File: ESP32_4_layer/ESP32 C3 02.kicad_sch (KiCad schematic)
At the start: 5 parts, among them J3 GSD090012SEU_SDcard_Connector, U2 ESP32-C3-WROOM-02, U3 CP2102N-Axx-xQFN20, U4 USBLC6-2SC6, U5 W25Q32JVSS

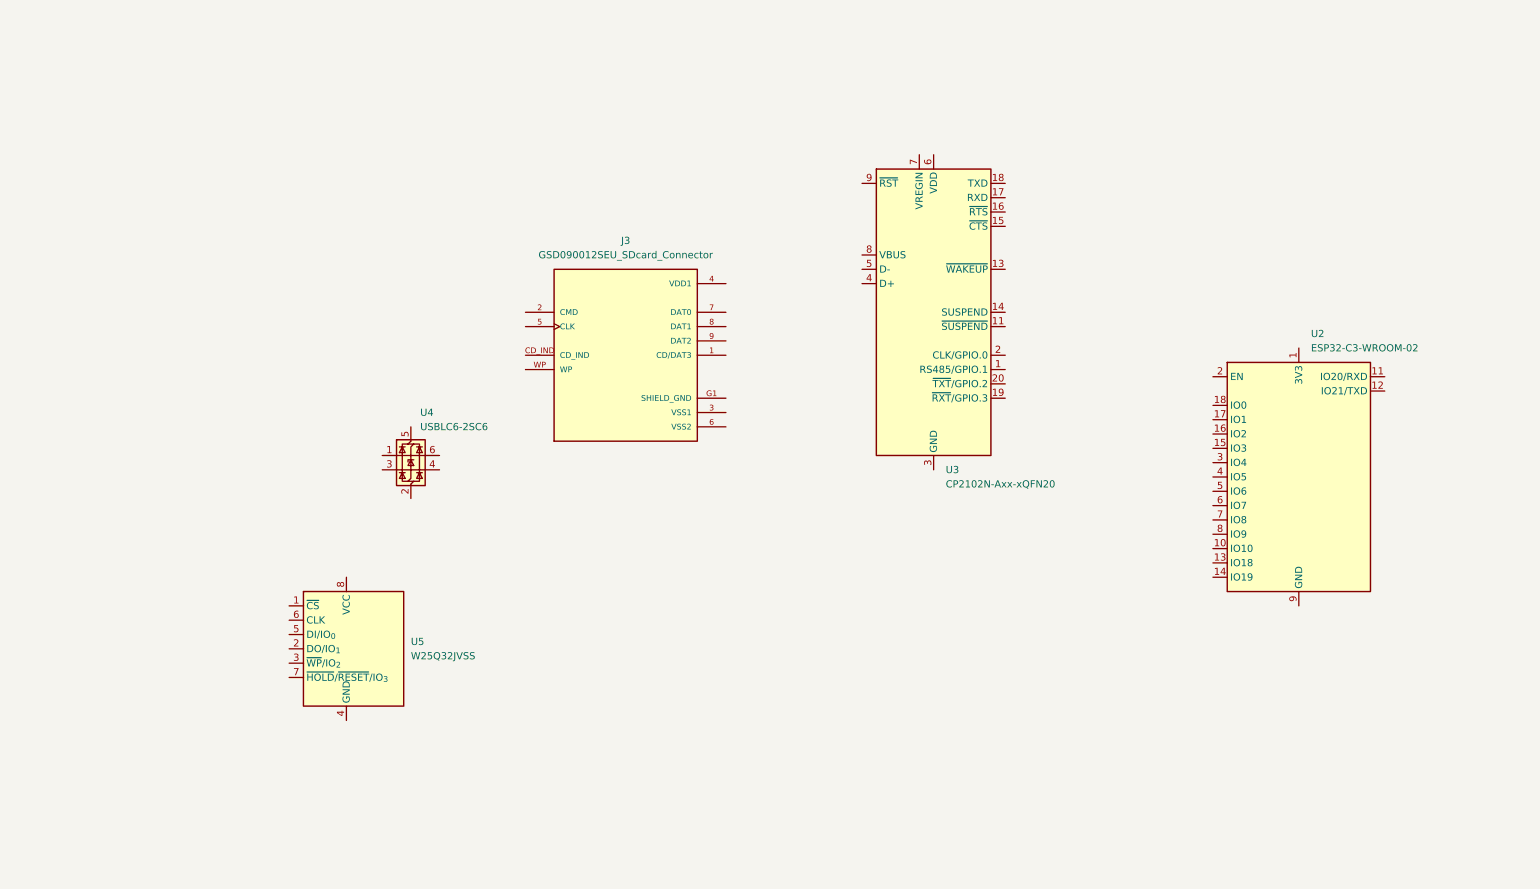
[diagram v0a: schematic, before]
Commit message: usb to uart converter schematic completed
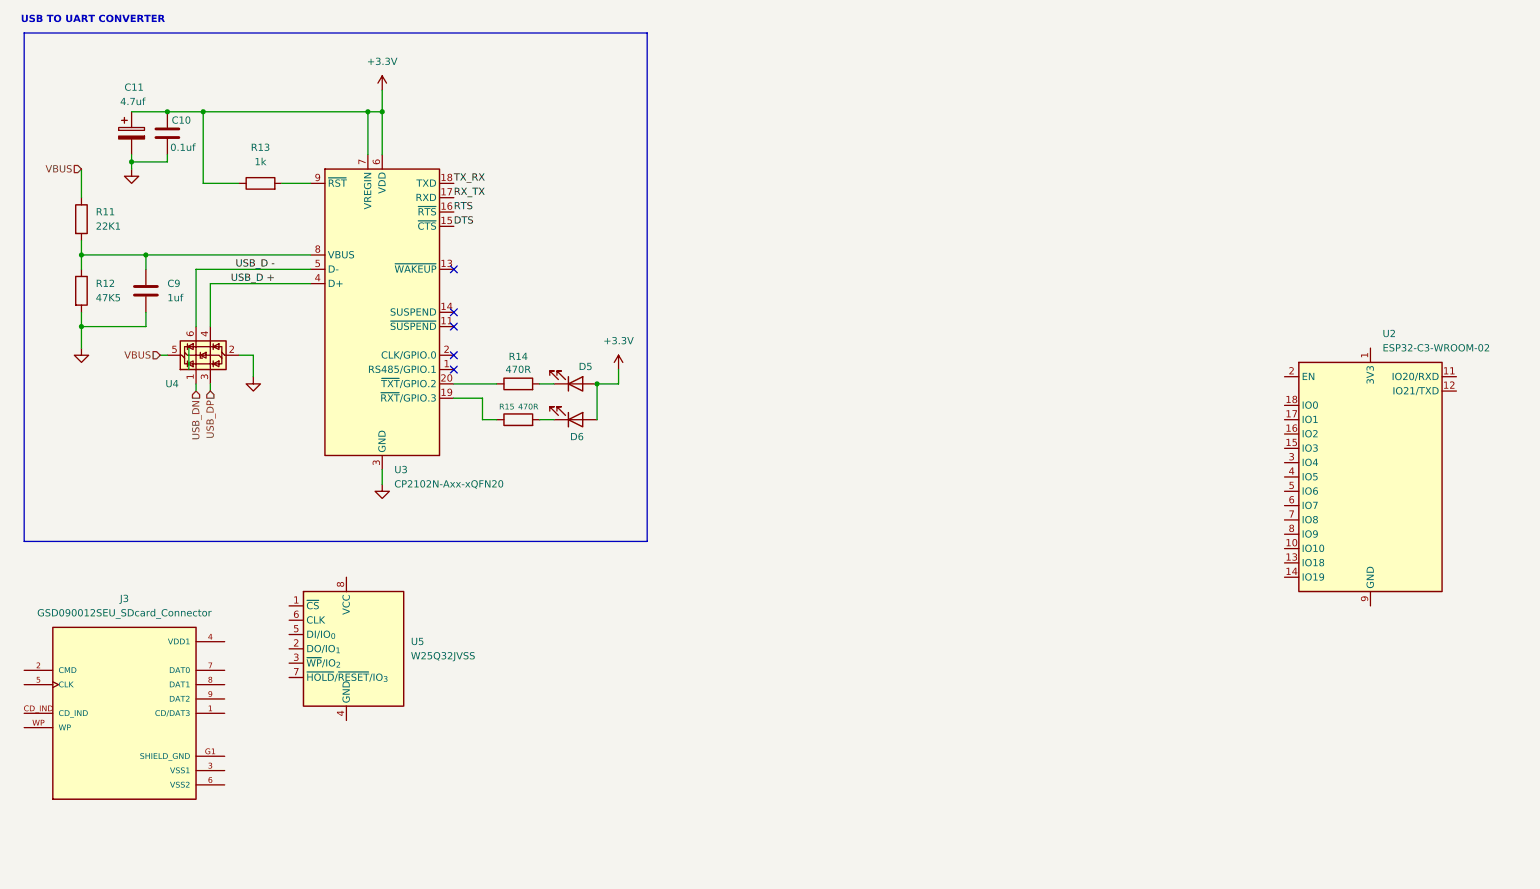
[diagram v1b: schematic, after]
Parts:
- added C10: 0.1uf, symbol Device:C
- added C11: 4.7uf, symbol Device:C_Polarized
- added C9: 1uf, symbol Device:C
- added D5, D6: LED, symbol Device:LED
- added R11: 22K1, symbol Device:R
- added R12: 47K5, symbol Device:R
- added R13: 1k, symbol Device:R
- added R14, R15: 470R, symbol Device:R
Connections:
- net GND: now reaches U3.12 (GND), U3.21 (GND), U3.3 (GND)
- net GND: now also U4.2 (GND), C10.2, C11.2, C9.2, R12.2
- net DTS: now reaches U3.15 (~{CTS})
- net RTS: now reaches U3.16 (~{RTS})
- net RX_TX: now reaches U3.17 (RXD)
- net TX_RX: now reaches U3.18 (TXD)
- net at U3.19 (~{RXT}/GPIO.3): now also R15.1
- net at U3.20 (~{TXT}/GPIO.2): now also R14.1
- net USB_D +: now reaches U3.4 (D+)
- net USB_D +: now also U4.4 (I/O2)
- net USB_D -: now reaches U3.5 (D-)
- net USB_D -: now also U4.6 (I/O1)
- net +3.3V: now reaches U3.6 (VDD)
- net +3.3V: now also U3.7 (VREGIN), C10.1, C11.1, D5.2 (A), D6.2 (A), R13.1
- net at U3.8 (VBUS): now also C9.1, R11.2, R12.1
- net at U3.9 (~{RST}): now also R13.2
- net USB_DN: now reaches U4.1 (I/O1)
- net USB_DP: now reaches U4.3 (I/O2)
- net VBUS: now reaches U4.5 (VBUS)
- net VBUS: now also R11.1
- new net: D5.1 (K), R14.2
- new net: D6.1 (K), R15.2
- no-connect marks 0 -> 5
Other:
- note added: "USB TO UART CONVERTER"
- moved on the sheet: J3, U2, U3, U4

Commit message: MCU and SD CARD schematic completed
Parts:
- removed U2: ESP32-C3-WROOM-02, RF_Module:ESP32-C3-WROOM-02, symbol RF_Module:ESP32-C3-WROOM-02
- added C12, C14: 10uf, symbol Device:C_Polarized
- added C13, C15: 0.1uf, symbol Device:C
- added R16: R15, symbol Device:R
- added R17, R19: 50R, symbol Device:R
- added R18: 10K, symbol Device:R
- added U2: ESP32-C3-WROOM-02-H4, ESP32-C3-WROOM-02-H4:MODULE_ESP32-C3-WROOM-02-H4, symbol Own_Library:ESP32-C3-WROOM-02-H4
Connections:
- net SHIELD_GND is gone; now on net GND: J3.G1 (SHIELD_GND), J3.G2 (SHIELD_GND), J3.G3 (SHIELD_GND), J3.G4 (SHIELD_GND)
- net +3.3V: now also J3.4 (VDD1), C12.1, C13.1, C14.1, C15.1, R18.2, U2.1 (3V3)
- net GND: now also J3.3 (VSS1), J3.6 (VSS2), J3.8 (DAT1), J3.9 (DAT2), C12.2, C13.2, C14.2, C15.2, U2.19 (GND), U2.20 (GND), U2.21 (GND), U2.22 (GND), U2.23 (GND), U2.24 (GND), U2.25 (GND), U2.26 (GND), U2.27 (GND), U2.28 (GND), U2.29 (GND), U2.30 (GND), U2.31 (GND), U2.32 (GND), U2.33 (GND), U2.34 (GND), U2.35 (GND), U2.36 (GND), U2.37 (GND), U2.38 (GND), U2.39 (GND), U2.9 (GND)
- net RX_TX: now also U2.12 (TXD)
- net TX_RX: now also U2.11 (RXD)
- net CS_SD: now reaches J3.1 (CD/DAT3)
- net CS_SD: now also U2.18 (IO0)
- net MOSI_DI: now reaches J3.2 (CMD)
- net MOSI_DI: now also R17.2
- net SCLK: now reaches J3.5 (CLK)
- net SCLK: now also R16.1
- net at J3.7 (DAT0): now also R19.1
- new net: R17.1, U2.6 (IO7)
- new net: R16.2, U2.5 (IO6)
- new net BOOT: U2.8 (IO9)
- new net CS: U2.10 (IO10)
- new net EN: U2.2 (EN)
- new net GPIO18: U2.13 (IO18)
- new net GPIO19: U2.14 (IO19)
- new net GPIO8: U2.7 (IO8)
- new net MIC_OUT: U2.4 (IO5)
- new net MISO_DO: R19.2, U2.16 (IO2)
- new net PHOTO_C: U2.17 (IO1)
- new net SCL: U2.15 (IO3)
- new net SDA: U2.3 (IO4)
- no-connect marks 5 -> 7
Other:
- note added: "MCU"
- note added: "SD CARD"
- moved on the sheet: J3, U5

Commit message: FLASH AND TEST POINTS
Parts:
- added C16: 0.1uf, symbol Device:C
- added R20: 50R, symbol Device:R
- added TP1, TP2, TP3, TP4, TP5: TestPoint, symbol Connector:TestPoint
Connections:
- net +3.3V: now also U5.3 (~{WP}/IO_{2}), U5.7 (~{HOLD}/~{RESET}/IO_{3}), U5.8 (VCC), C16.1
- net CS: now also U5.1 (~{CS}), TP4.1
- net CS_SD: now also TP5.1
- net GND: now also U5.4 (GND), C16.2
- net MISO_DO: now also R20.1, TP1.1
- net MOSI_DI: now also U5.5 (DI/IO_{0}), TP2.1
- net SCLK: now also U5.6 (CLK), TP3.1
- net at U5.2 (DO/IO_{1}): now also R20.2
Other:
- added sheet Sensors (Sensors.kicad_sch)
- added sheet User Interface (User_Interface.kicad_sch)
- note added: "FLASH MEMORY"
- note added: "TEST POINTS"
- title: (none) -> ESP32 C3, USB to UART, SD CARD and FLASH
- moved on the sheet: C15, U5

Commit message: SENSORS COMPLETED
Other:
- sheet Sensors ports: added MIC_OUT, PHOTO_C, SCL, SDA; removed none
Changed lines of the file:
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@@
 	(wire
 		(pts
+			(xy 262.89 125.73) (xy 260.35 125.73)
+		)
+		(stroke
+			(width 0)
+			(type default)
+		)
+	)
+	(wire
+		(pts
 			(xy 205.74 156.21) (xy 205.74 152.4)
 		)
@@
 	(wire
 		(pts
+			(xy 262.89 133.35) (xy 260.35 133.35)
+		)
+		(stroke
+			(width 0)
+			(type default)
+		)
+	)
+	(wire
+		(pts
 			(xy 203.2 48.26) (xy 210.82 48.26)
 		)
@@
 	(wire
 		(pts
+			(xy 262.89 128.27) (xy 260.35 128.27)
+		)
+		(stroke
+			(width 0)
+			(type default)
+		)
+	)
+	(wire
+		(pts
 			(xy 48.26 41.91) (xy 48.26 43.18)
 		)
@@
 	(wire
 		(pts
+			(xy 262.89 130.81) (xy 260.35 130.81)
+		)
+		(stroke
+			(width 0)
+			(type default)
+		)
+	)
+	(wire
+		(pts
 			(xy 48.26 34.29) (xy 54.61 34.29)
 		)
@@
 		)
 	)
+	(label "SDA"
+		(at 262.89 133.35 0)
+		(effects
+			(font
+				(size 1.27 1.27)
+				(thickness 0.254)
+				(bold yes)
+			)
+			(justify left bottom)
+		)
+	)
+	(label "MIC_OUT"
+		(at 262.89 125.73 0)
+		(effects
+			(font
+				(size 1.27 1.27)
+				(thickness 0.254)
+				(bold yes)
+			)
+			(justify left bottom)
+		)
+	)
 	(label "GPIO18"
 		(at 203.2 58.42 0)
@@
 		)
 	)
+	(label "SCL"
+		(at 262.89 130.81 0)
+		(effects
+			(font
+				(size 1.27 1.27)
+				(thickness 0.254)
+				(bold yes)
+			)
+			(justify left bottom)
+		)
+	)
 	(label "MOSI_DI"
 		(at 219.71 48.26 0)
@@
 		)
 	)
+	(label "PHOTO_C"
+		(at 262.89 128.27 0)
+		(effects
+			(font
+				(size 1.27 1.27)
+				(thickness 0.254)
+				(bold yes)
+			)
+			(justify left bottom)
+		)
+	)
 	(label "MISO_DO"
 		(at 167.64 53.34 180)
@@
 	)
 	(sheet
-		(at 243.84 146.05)
+		(at 246.38 144.78)
 		(size 13.97 12.7)
 		(exclude_from_sim no)
@@
 		)
 		(property "Sheetname" "User Interface"
-			(at 243.84 145.3384 0)
+			(at 246.38 144.0684 0)
 			(effects
 				(font
@@
 		)
 		(property "Sheetfile" "User_Interface.kicad_sch"
-			(at 243.84 159.3346 0)
+			(at 246.38 158.0646 0)
 			(effects
 				(font
@@
 	)
 	(sheet
-		(at 242.57 123.19)
+		(at 246.38 123.19)
 		(size 13.97 12.7)
 		(exclude_from_sim no)
@@
 		)
 		(fill
-			(color 37 17 255 1.0000)
+			(color 39 252 255 1.0000)
 		)
 		(property "Sheetname" "Sensors"
-			(at 242.57 122.4784 0)
+			(at 246.38 122.4784 0)
 			(effects
 				(font
@@
 		)
 		(property "Sheetfile" "Sensors.kicad_sch"
-			(at 242.57 136.4746 0)
+			(at 246.38 136.4746 0)
 			(effects
 				(font
@@
 			)
 		)
+		(pin "MIC_OUT" output
+			(at 260.35 125.73 0)
+			(effects
+				(font
+					(size 1.27 1.27)
+				)
+				(justify right)
+			)
+		)
+		(pin "PHOTO_C" output
+			(at 260.35 128.27 0)
+			(effects
+				(font
+					(size 1.27 1.27)
+				)
+				(justify right)
+			)
+		)
+		(pin "SCL" input
+			(at 260.35 130.81 0)
+			(effects
+				(font
+					(size 1.27 1.27)
+				)
+				(justify right)
+			)
+		)
+		(pin "SDA" input
+			(at 260.35 133.35 0)
+			(effects
+				(font
+					(size 1.27 1.27)
+				)
+				(justify right)
+			)
+		)

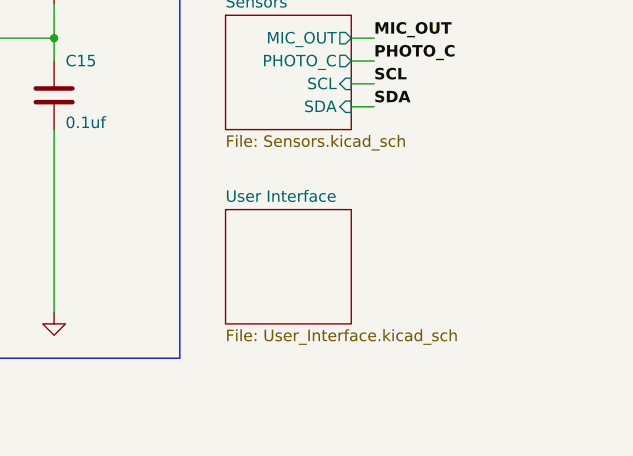
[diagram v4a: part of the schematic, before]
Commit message: hierarchial label attached
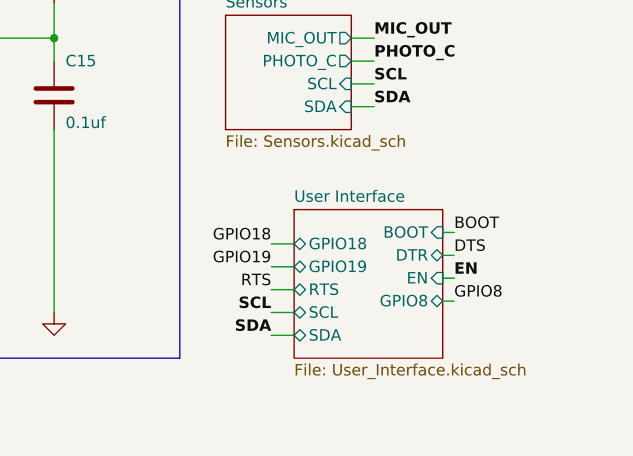
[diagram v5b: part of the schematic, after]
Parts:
- C10, C13, C15, C16, C9: footprint (none) -> Capacitor_SMD:C_0805_2012Metric
- C11, C12, C14: footprint (none) -> Own_Library:T491A_Tantalum_Capacitor
- D5: footprint (none) -> Own_Library:Blue_Led_
- D6: footprint (none) -> Own_Library:Red_Led
- R11, R12, R13, R14, R15, R16, R17, R18, R19, R20: footprint (none) -> Resistor_SMD:R_0805_2012Metric
- TP1, TP2, TP3, TP4, TP5: footprint (none) -> TestPoint:TestPoint_Pad_D1.0mm
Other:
- sheet User Interface ports: added BOOT, DTR, EN, GPIO18, GPIO19, GPIO8, RTS, SCL, SDA; removed none

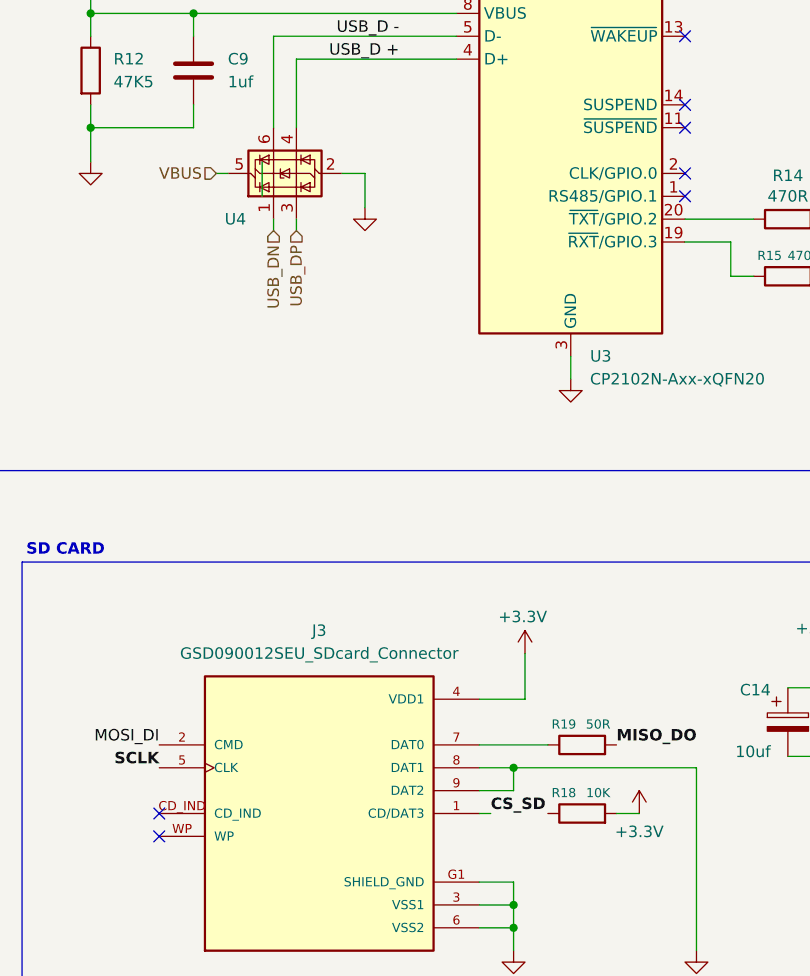
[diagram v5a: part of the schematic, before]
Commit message: PCB Stack up, netlist and constrainsts applied
Signed-off-by: jayaraj <jayarajemengineer@gmail.com>
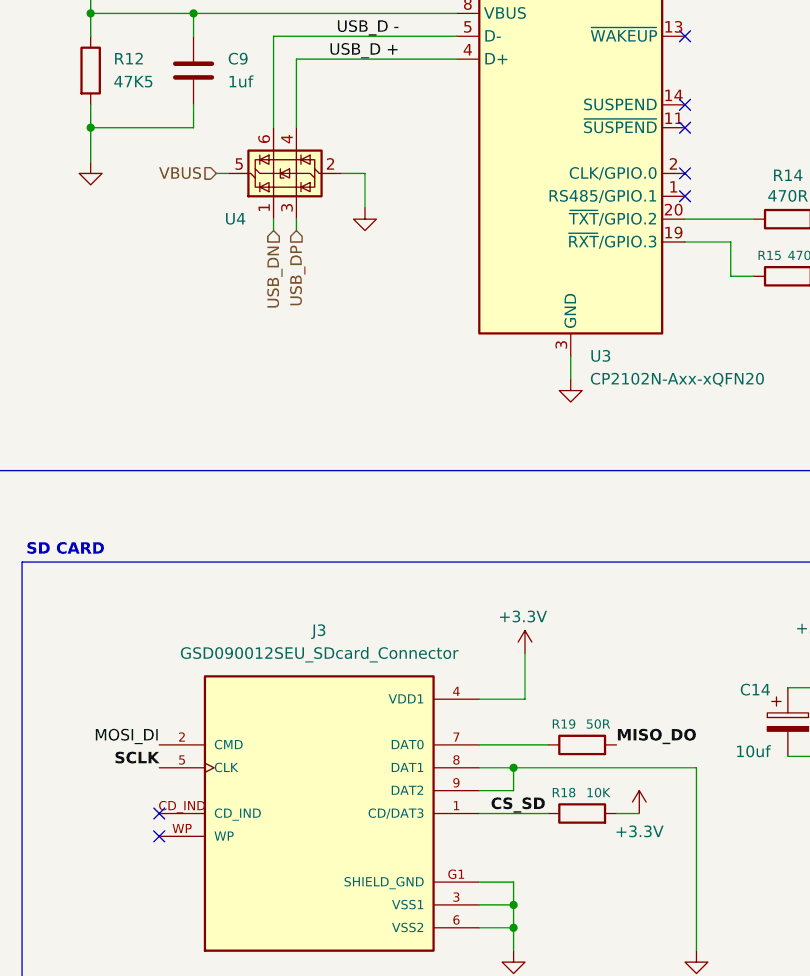
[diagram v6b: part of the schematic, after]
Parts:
- J3: footprint GSD090012SEU:AMPHENOL_GSD090012SEU -> Own_Library:GSD090012SEU_SDCard_connector
- U2: footprint ESP32-C3-WROOM-02-H4:MODULE_ESP32-C3-WROOM-02-H4 -> Own_Library:ESP32-C3-WROOM-02-H4
- U3: footprint Package_DFN_QFN:SiliconLabs_QFN-20-1EP_3x3mm_P0.5mm -> Own_Library:QFN20_CP2102N_SIL
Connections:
- net CS_SD: now also R18.1
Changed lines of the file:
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@@
 	(wire
 		(pts
-			(xy 77.47 148.59) (xy 76.2 148.59)
+			(xy 76.2 148.59) (xy 83.82 148.59)
 		)
 		(stroke
@@
 	(wire
 		(pts
-			(xy 52.07 76.2) (xy 52.07 80.01)
-		)
-		(stroke
-			(width 0)
-			(type default)
-		)
-	)
-	(wire
-		(pts
 			(xy 262.89 130.81) (xy 260.35 130.81)
 		)
@@
 			)
 		)
-		(property "Footprint" "Package_DFN_QFN:SiliconLabs_QFN-20-1EP_3x3mm_P0.5mm"
+		(property "Footprint" "Own_Library:QFN20_CP2102N_SIL"
 			(at 118.11 96.52 0)
 			(effects
@@
 			)
 		)
-		(property "Footprint" "GSD090012SEU:AMPHENOL_GSD090012SEU"
+		(property "Footprint" "Own_Library:GSD090012SEU_SDCard_connector"
 			(at 58.42 148.59 0)
 			(effects
@@
 			)
 		)
-		(property "Footprint" "ESP32-C3-WROOM-02-H4:MODULE_ESP32-C3-WROOM-02-H4"
+		(property "Footprint" "Own_Library:ESP32-C3-WROOM-02-H4"
 			(at 185.42 58.42 0)
 			(effects
